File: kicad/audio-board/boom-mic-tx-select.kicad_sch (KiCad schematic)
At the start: 6 parts, among them J4 BOOM_MIC_FROM_EARCUP, J5 TRS_TO_PJ068_AIRCRAFT, K1 G6K-2F-Y, Q1 2N7002

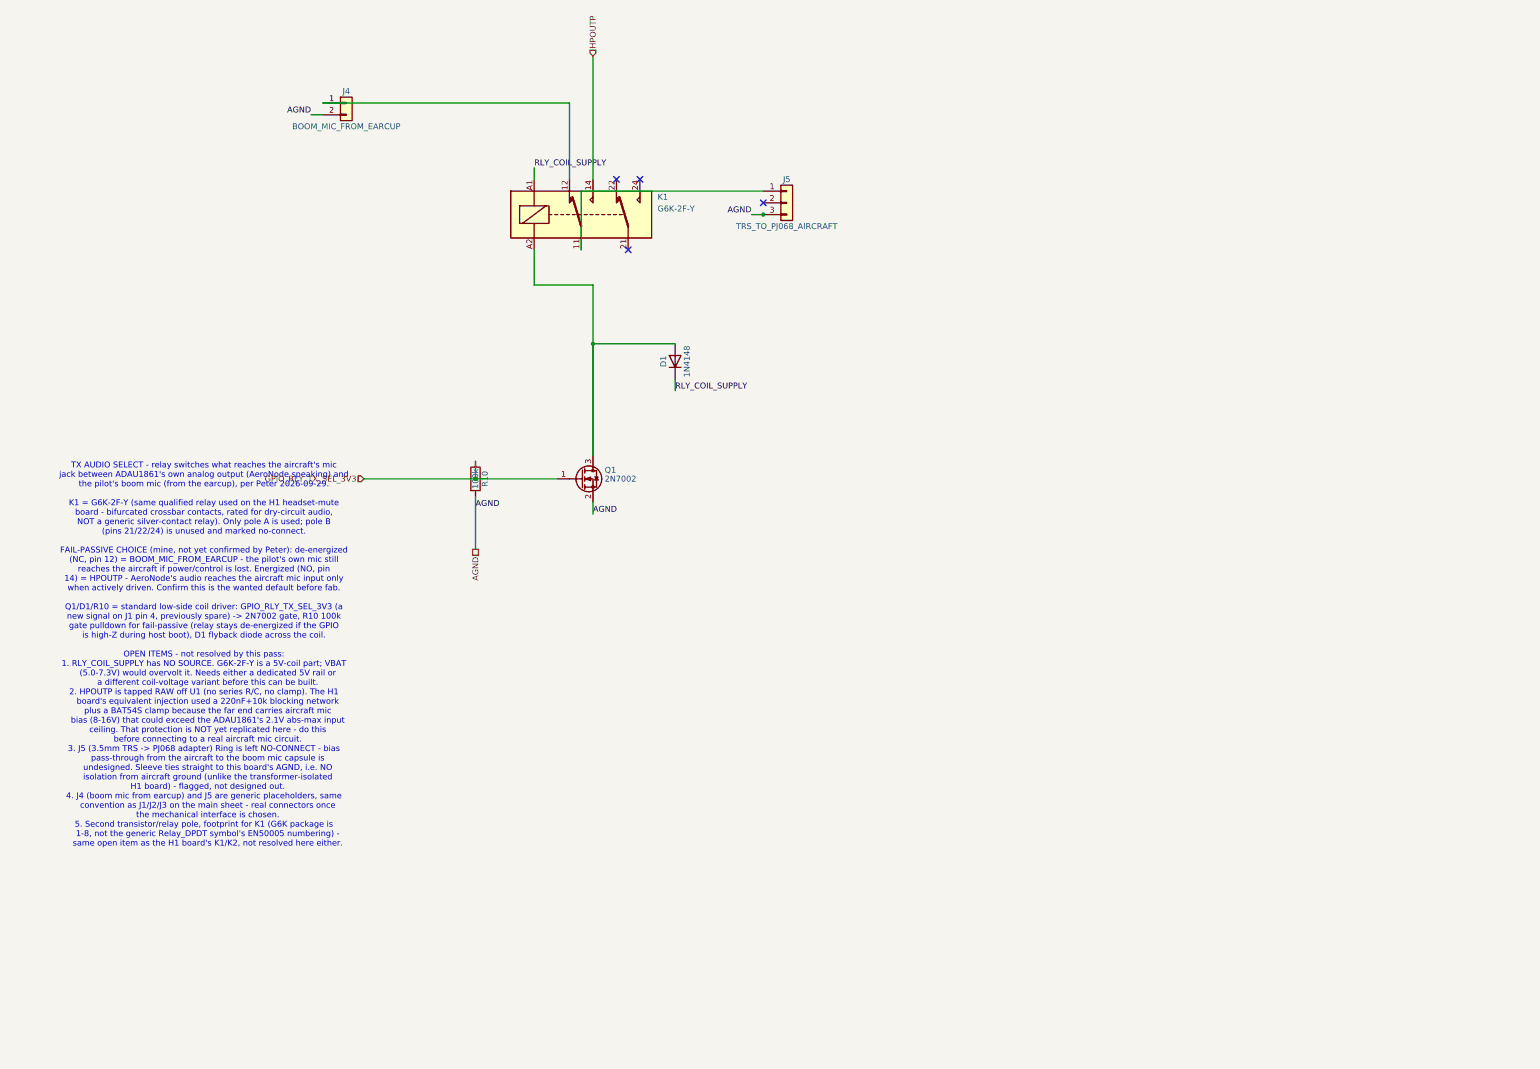
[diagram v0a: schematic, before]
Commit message: [LIMA] resolve relay coil supply: U11 regulates VBAT to 4.5V, per Peter's option 1
Fetched Omron's G6K datasheet (not cached anywhere in this repo before
now) to settle the open item from the previous commit. Checked all five
stock G6K-2F-Y coil options (3/4.5/5/12/24 VDC) against VBAT's 5.0-7.3V
swing: none spans it cleanly for continuous duty. The 5V coil is the
only contender, but VBAT_max (146% of rated) sits right at a rating the
datasheet explicitly says is instantaneous-only, not continuous.

Peter ruled option 1 of 4 (dedicated regulator, vs. a PWM coil
economiser / different relay / borrowing a 5V rail from aeronode).

Added U11 - the SAME ADP7118AUJZ-1.8-R7 already used twice on this
board as U9/U10, wired in its adjustable configuration (R11 15k / R12
10k per the datasheet's own Fig. 39 formula) instead of the fixed
pass-through, to produce a 4.5V RLY_COIL_SUPPLY rail: safely above the
5V coil's 80%-of-rated guaranteed-operate floor, and independent of
VBAT's swing entirely. New VBAT sheet pin added to carry the supply in.

Caught two more of the same collinear-wire short bug this sheet's
initial relay routing hit: the VOUT-to-divider and SENSE/ADJ-to-divider
runs both crossed straight through other pins on their way to R11/R12
because the auto-router's L-path shared a column with the divider
stack. Both rerouted with dogleg paths after ERC/find_shorted_nets
caught them.

Also caught and fixed a real legibility bug in the design-note text
objects: they're center-anchored on both axes (not top-left as
assumed), so the first draft's note ran off the child sheet's edges
and overlapped its own components. Bumped the child sheet to A3 (was
undersized A4 for this much documentation) and repositioned.

Verified: ERC errors unchanged at 46 (no new unconnected pins), 0
shorted nets, 0 overlaps across both sheets, rendered and visually
checked.

Co-Authored-By: Claude Sonnet 5 <noreply@anthropic.com>
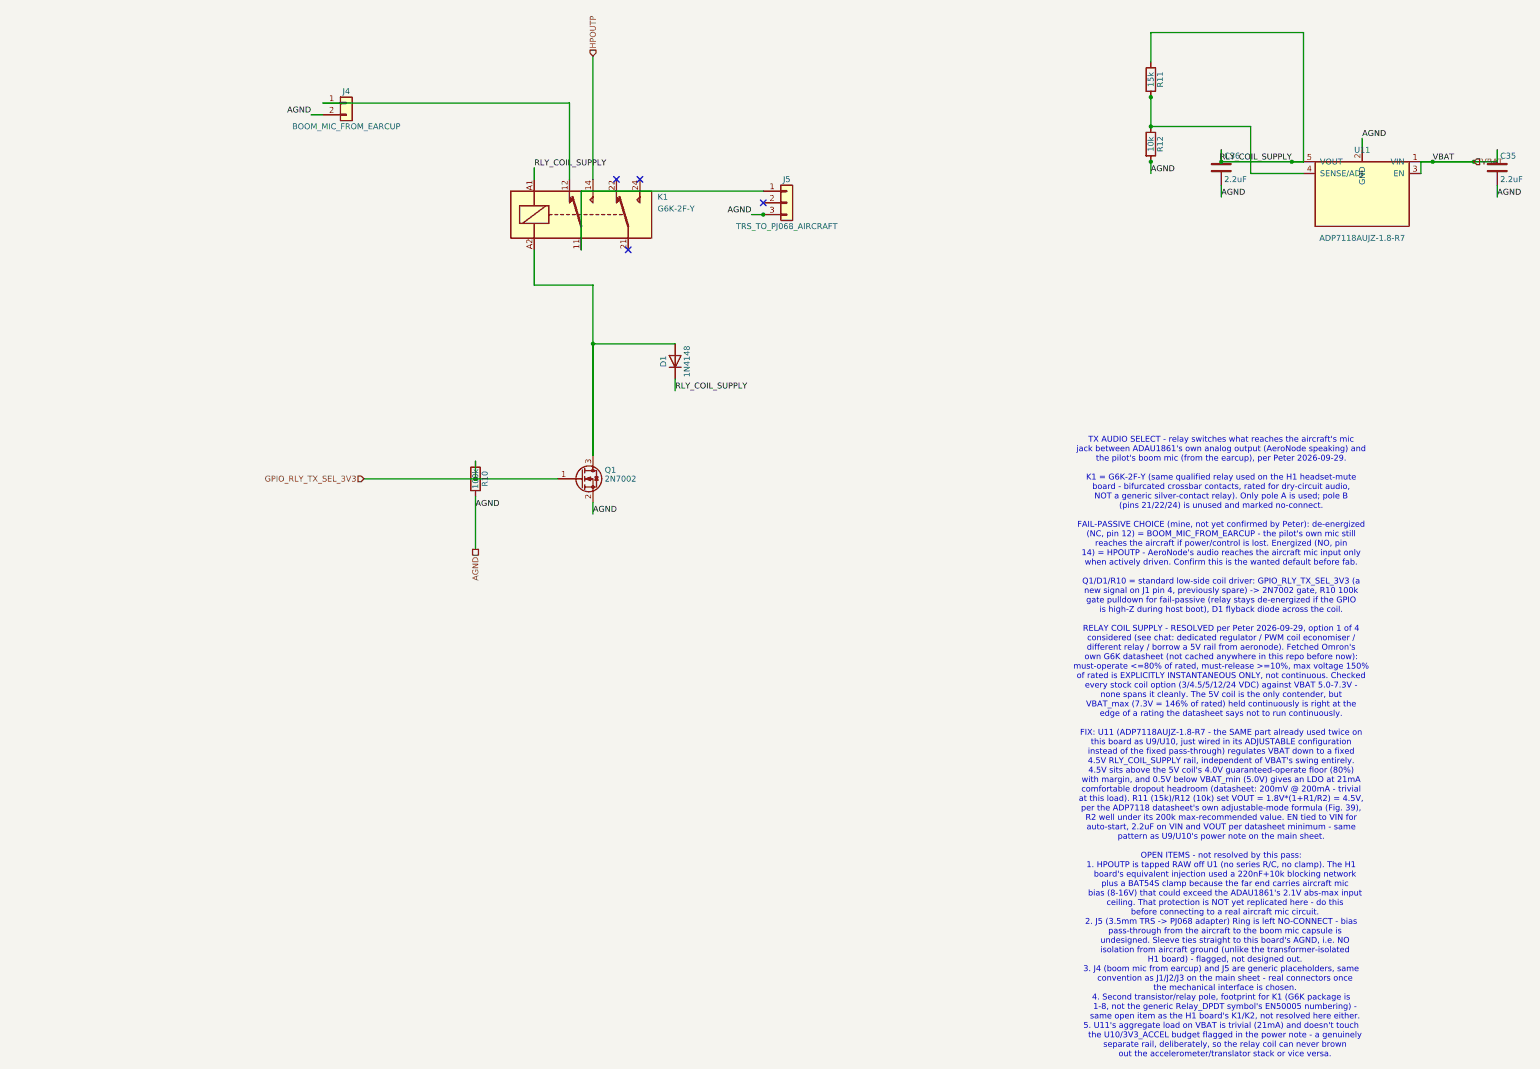
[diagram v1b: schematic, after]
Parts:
- added C35, C36: 2.2uF, symbol Device:C
- added R11: 15k, symbol Device:R
- added R12: 10k, symbol Device:R
- added U11: ADP7118AUJZ-1.8-R7, symbol AnalogDevices:ADP7118
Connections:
- net AGND: now also C35.2, C36.2, R12.2, U11.2 (GND)
- net RLY_COIL_SUPPLY: now also C36.1, R11.1, U11.5 (VOUT)
- new net: R11.2, R12.1, U11.4 (SENSE/ADJ)
- new net VBAT: C35.1, U11.1 (VIN), U11.3 (EN)

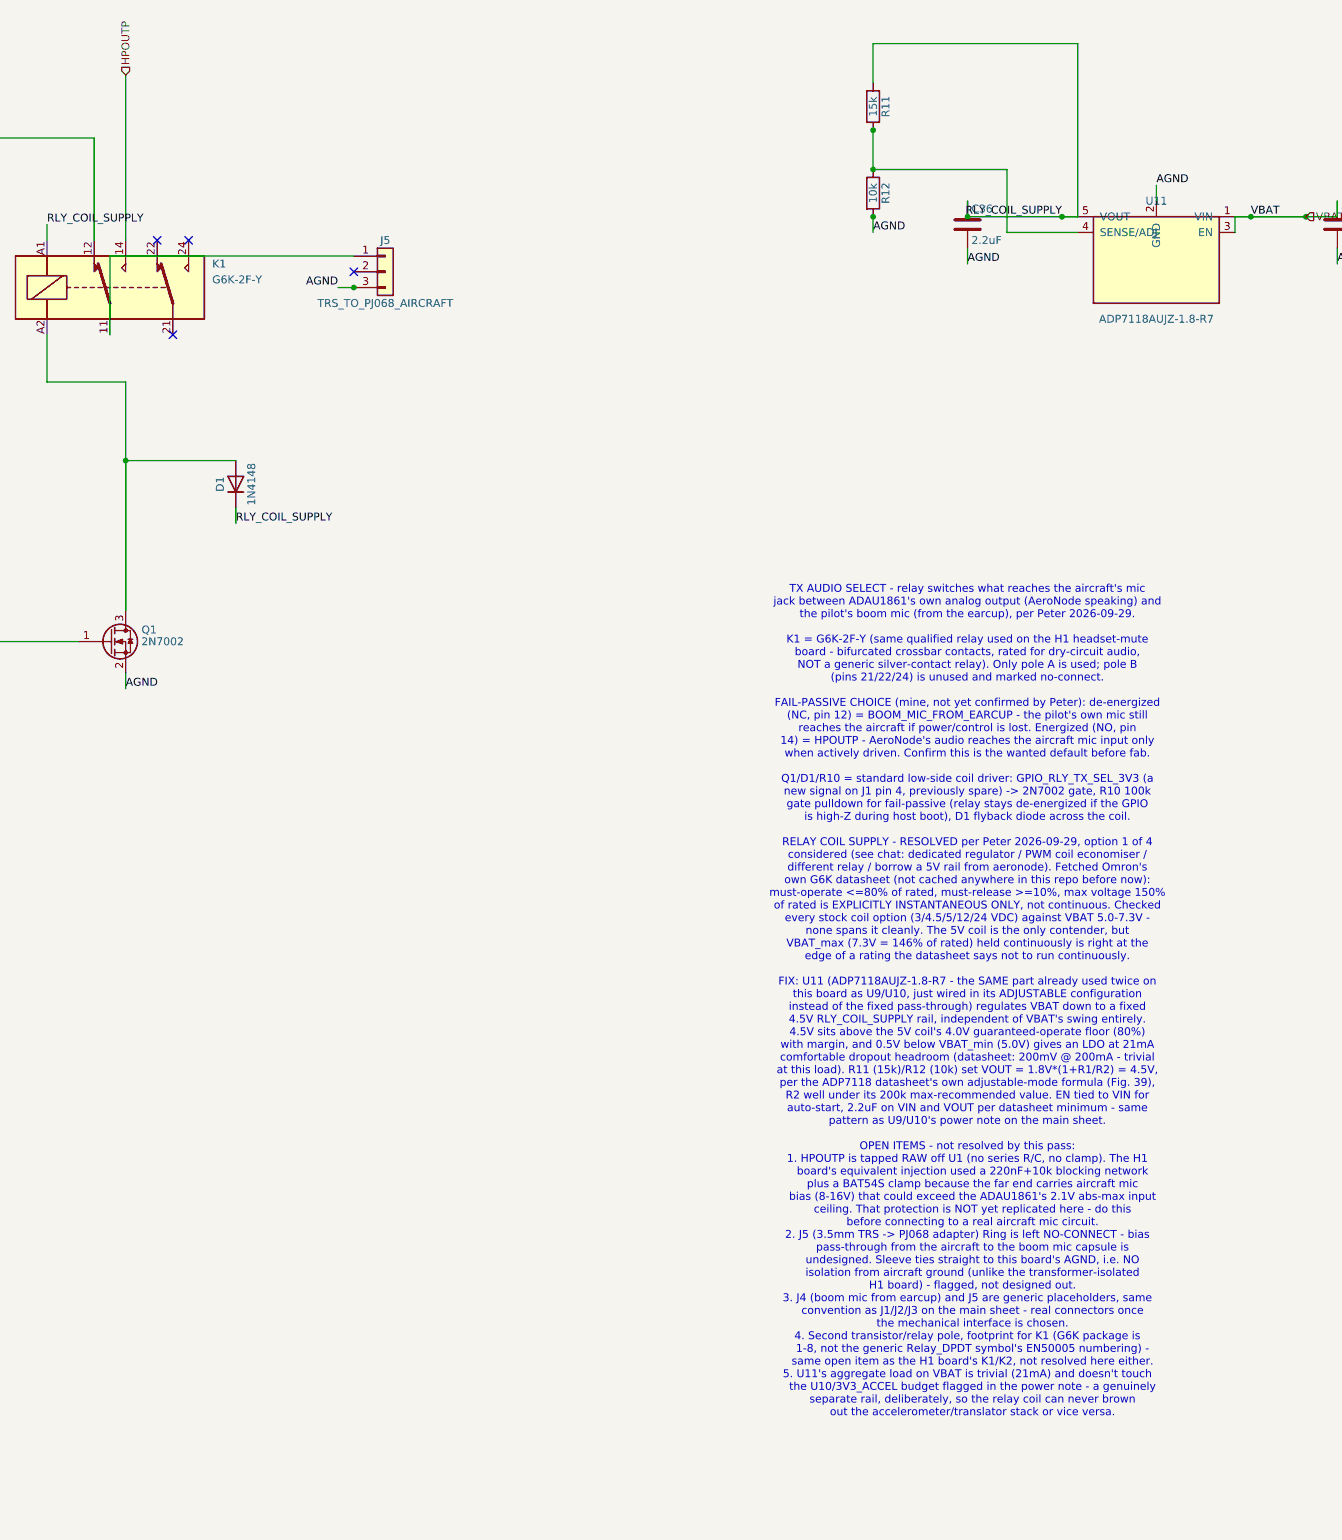
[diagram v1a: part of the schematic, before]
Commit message: [LIMA] add HPOUTP blocking cap + BAT54S clamp, same topology as the H1 board
Resolves the second open item from the previous commit. HPOUTP now
runs through C37 (220nF, C0G/film - not X7R, whose DC-bias derating
would walk the corner into the voice band) then R13 (10k) before
reaching the relay's NO_A contact, with D2 (BAT54S) clamping that
node between AGND and 1V8. Reused the H1 headset-mute board's mic-
line injection topology (its section 10.1) rather than re-deriving
it: R13 after C37 so a shorted cap can't pass more than a resistor-
limited fault current, same reasoning as that board's R1.

Clamp rails are 1V8/AGND specifically because that tracks the
ADAU1861's own abs-max spec ("Analog Input Voltage (Signal Pins)
-0.3V to AVDD+0.3V") rather than an arbitrary value - if AVDD ever
changes, the clamp tracks it by construction. New 1V8 sheet pin
added to carry the rail in from the main sheet's U9 output.

Caught and fixed a label-crowding legibility issue: the new D2/AGND
net label and the pre-existing J5/AGND label were both pointing
toward each other on the same row and overlapping in the render.
Moved one further out.

Verified: ERC errors unchanged at 46, 0 shorted nets, 0 overlaps,
rendered and visually checked.

Co-Authored-By: Claude Sonnet 5 <noreply@anthropic.com>
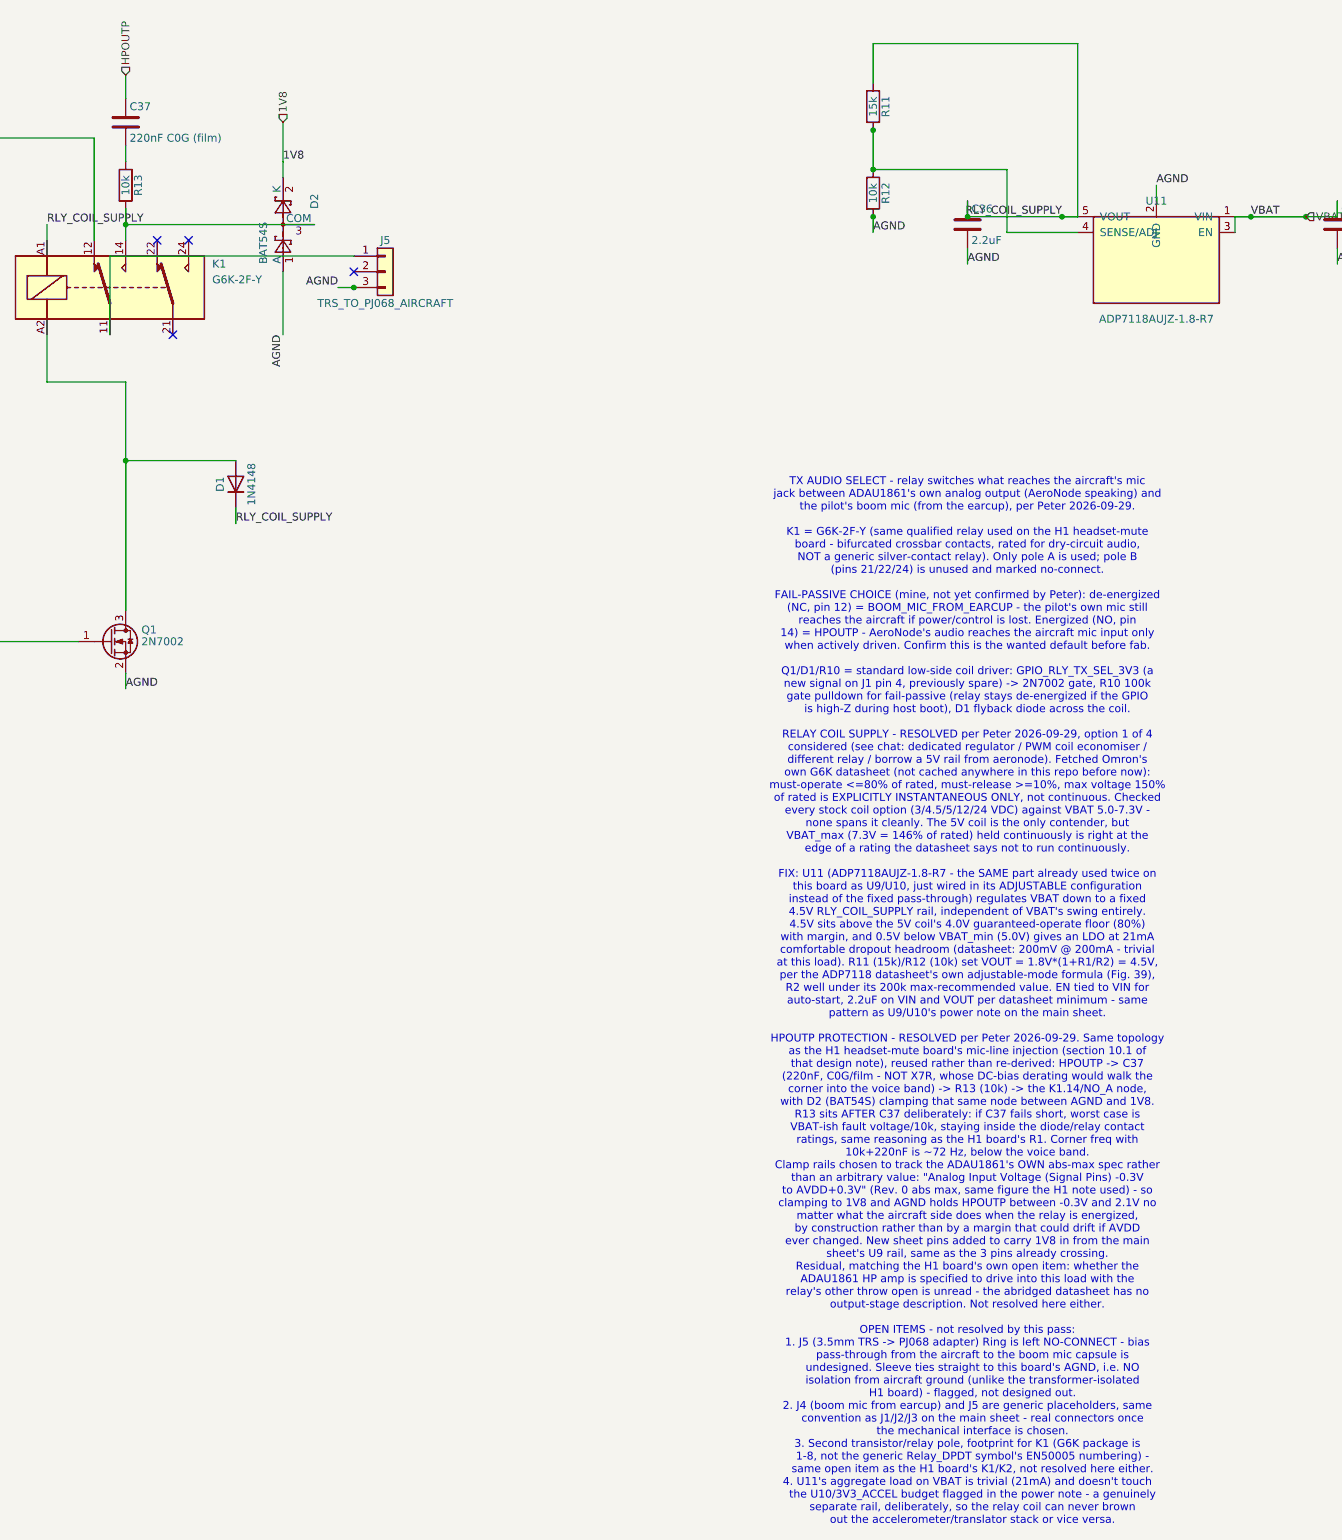
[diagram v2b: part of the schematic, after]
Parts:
- added C37: 220nF C0G (film), symbol Device:C
- added D2: BAT54S, symbol Diode:BAT54S
- added R13: 10k, symbol Device:R
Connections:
- net AGND: now also D2.1 (A)
- net HPOUTP: now also C37.1; no longer K1.14
- new net: D2.3 (COM), K1.14, R13.2
- new net: C37.2, R13.1
- new net 1V8: D2.2 (K)
